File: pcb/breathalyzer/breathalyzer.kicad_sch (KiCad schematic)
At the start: 29 parts, among them J1 Conn_01x07_Pin, J2 MP-3B socket, Q1 Q_PMOS, Q2 NPN, SW1 PTS636SK43SMTR, SW2 430162085826, U1 STM32F030K6Tx, U2 TLV73325PDBV, U4 TLV61070ADBV, U5 AY0438X-L

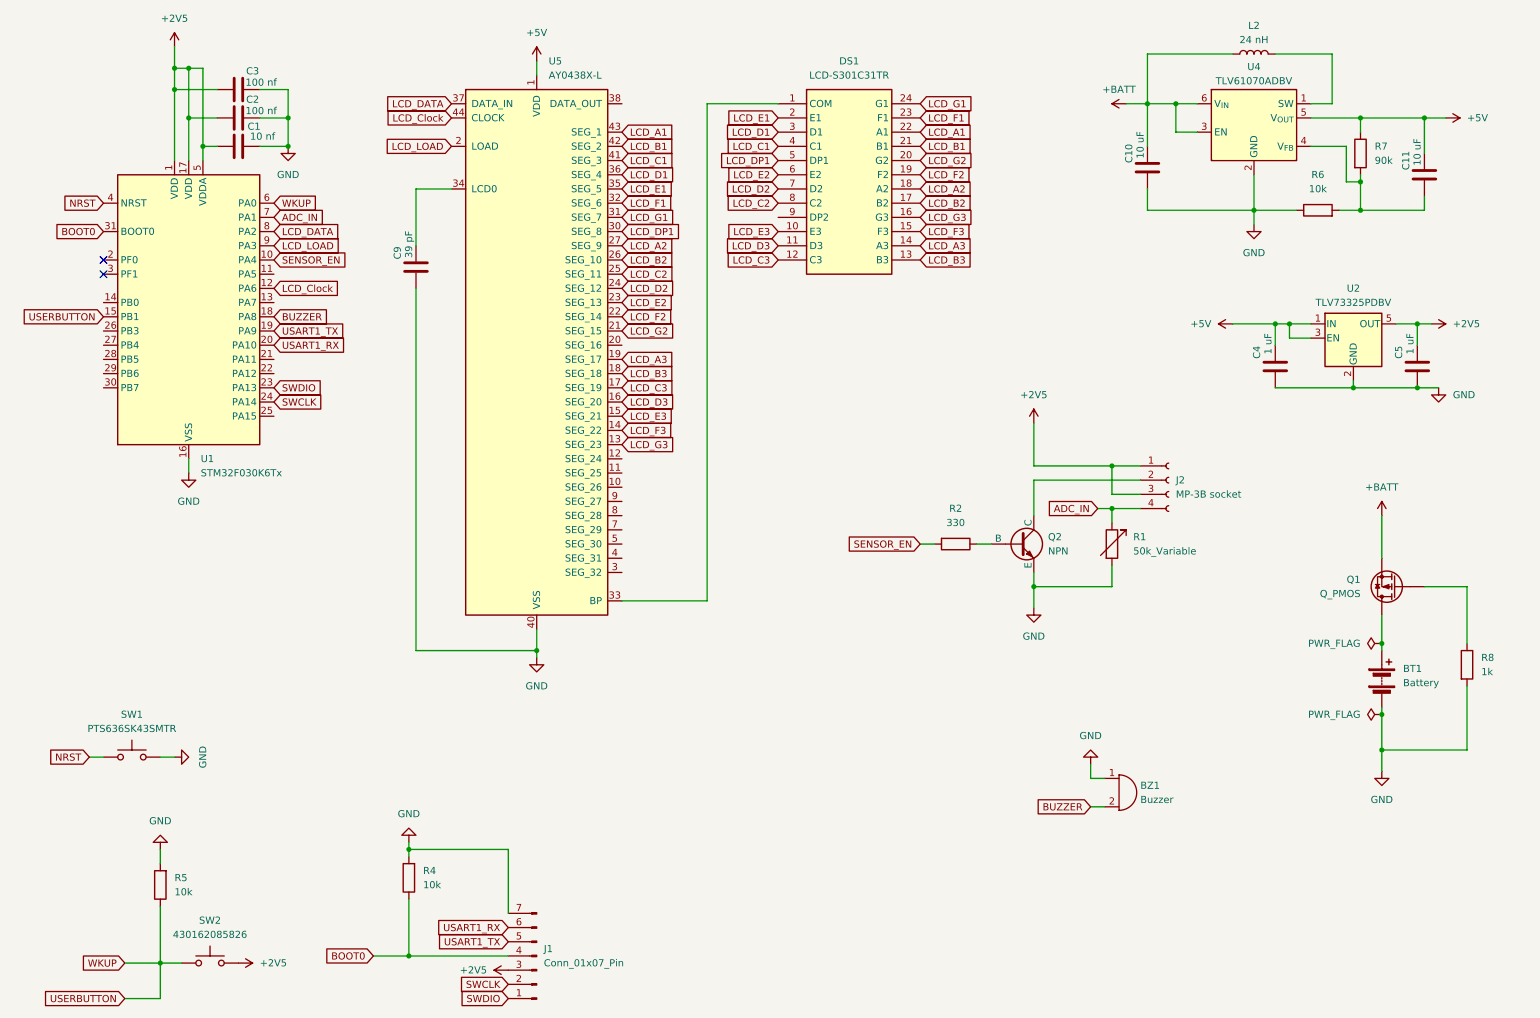
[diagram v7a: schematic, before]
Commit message: finalized schematic
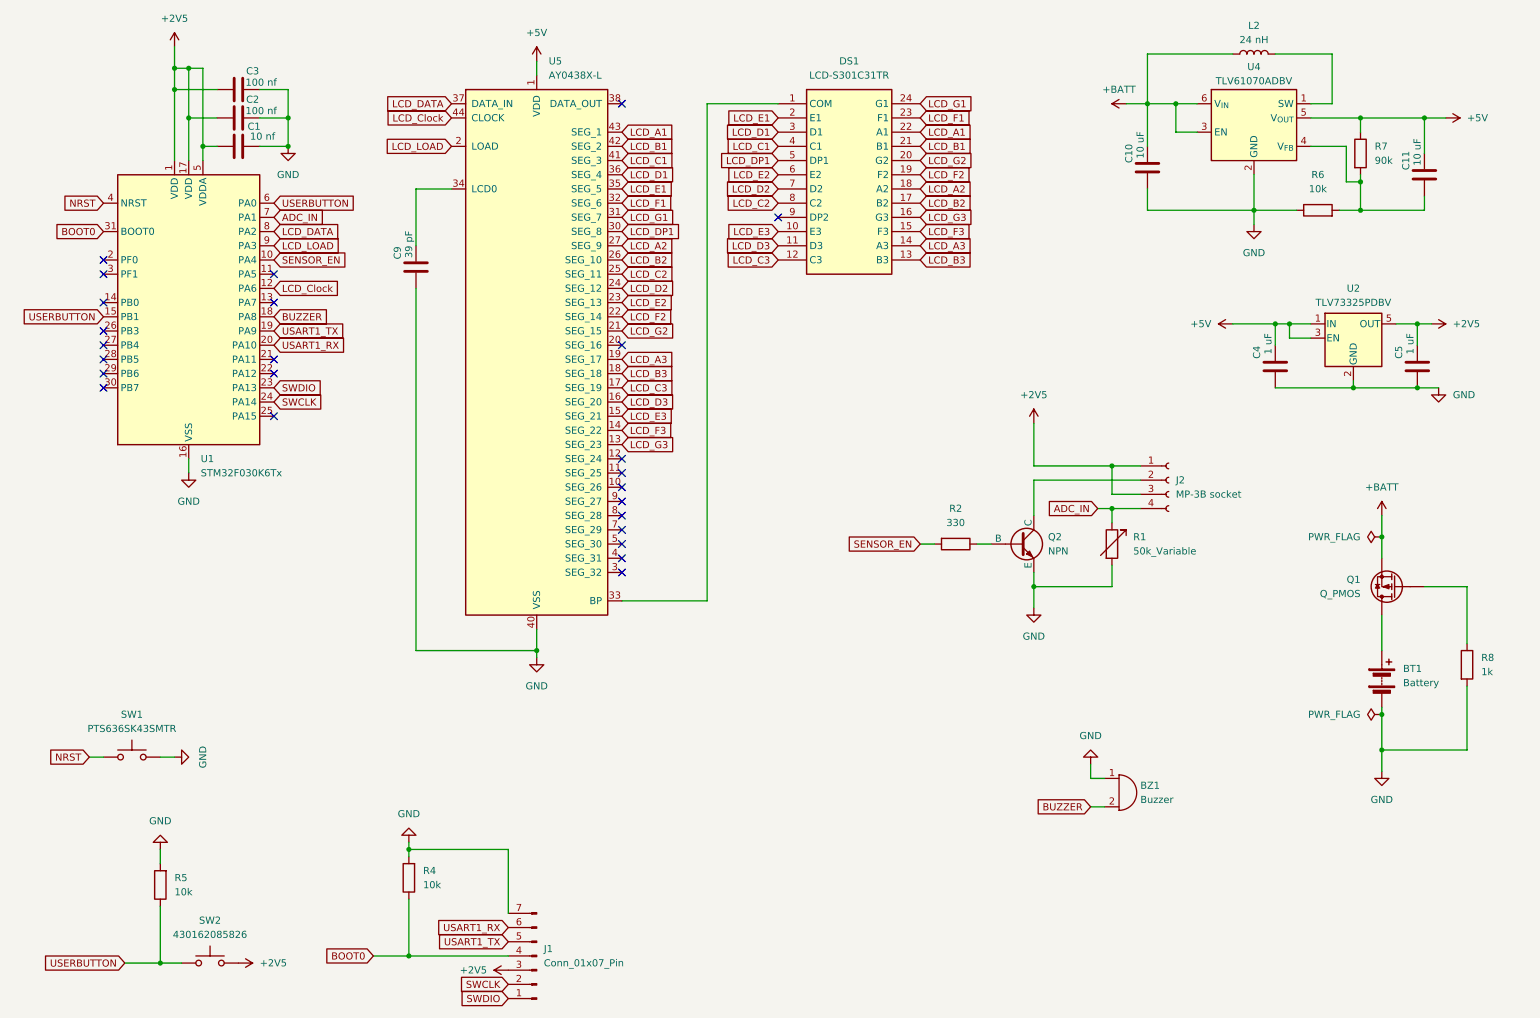
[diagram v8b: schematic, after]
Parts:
- DS1: footprint LCD-S301C31TR -> breathalyzer:LCD-S301C31TR
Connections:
- no-connect marks 2 -> 25
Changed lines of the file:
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@@
 	)
 	(junction
+		(at 257.81 106.68)
+		(diameter 0)
+		(color 0 0 0 0)
+	)
+	(junction
 		(at 195.58 115.57)
 		(diameter 0)
@@
 	)
 	(junction
-		(at 257.81 125.73)
-		(diameter 0)
-		(color 0 0 0 0)
-	)
-	(junction
 		(at 209.55 101.6)
 		(diameter 0)
@@
 	)
 	(no_connect
+		(at 121.92 110.49)
+	)
+	(no_connect
+		(at 121.92 72.39)
+	)
+	(no_connect
+		(at 59.69 77.47)
+	)
+	(no_connect
+		(at 121.92 92.71)
+	)
+	(no_connect
+		(at 121.92 95.25)
+	)
+	(no_connect
 		(at 29.21 59.69)
 	)
 	(no_connect
+		(at 121.92 29.21)
+	)
+	(no_connect
+		(at 29.21 69.85)
+	)
+	(no_connect
+		(at 29.21 72.39)
+	)
+	(no_connect
+		(at 121.92 100.33)
+	)
+	(no_connect
+		(at 149.86 49.53)
+	)
+	(no_connect
+		(at 59.69 59.69)
+	)
+	(no_connect
+		(at 59.69 64.77)
+	)
+	(no_connect
+		(at 121.92 113.03)
+	)
+	(no_connect
+		(at 29.21 64.77)
+	)
+	(no_connect
 		(at 29.21 57.15)
 	)
+	(no_connect
+		(at 59.69 85.09)
+	)
+	(no_connect
+		(at 29.21 77.47)
+	)
+	(no_connect
+		(at 29.21 74.93)
+	)
+	(no_connect
+		(at 59.69 74.93)
+	)
+	(no_connect
+		(at 121.92 107.95)
+	)
+	(no_connect
+		(at 121.92 102.87)
+	)
+	(no_connect
+		(at 121.92 105.41)
+	)
+	(no_connect
+		(at 121.92 97.79)
+	)
+	(no_connect
+		(at 29.21 80.01)
+	)
 	(wire
 		(pts
@@
 	(wire
 		(pts
-			(xy 257.81 125.73) (xy 257.81 127)
-		)
-		(stroke
-			(width 0)
-			(type default)
-		)
-	)
-	(wire
-		(pts
 			(xy 215.9 48.26) (xy 234.95 48.26)
 		)
@@
 	(wire
 		(pts
-			(xy 33.02 182.88) (xy 39.37 182.88)
-		)
-		(stroke
-			(width 0)
-			(type default)
-		)
-	)
-	(wire
-		(pts
 			(xy 39.37 182.88) (xy 43.18 182.88)
 		)
@@
 	(wire
 		(pts
-			(xy 33.02 189.23) (xy 39.37 189.23)
-		)
-		(stroke
-			(width 0)
-			(type default)
-		)
-	)
-	(wire
-		(pts
-			(xy 39.37 189.23) (xy 39.37 182.88)
+			(xy 33.02 182.88) (xy 39.37 182.88)
 		)
 		(stroke
@@
 	(wire
 		(pts
-			(xy 257.81 120.65) (xy 257.81 125.73)
+			(xy 257.81 120.65) (xy 257.81 127)
 		)
 		(stroke
@@
 	(wire
 		(pts
-			(xy 257.81 102.87) (xy 257.81 110.49)
+			(xy 257.81 102.87) (xy 257.81 106.68)
 		)
 		(stroke
@@
 	(wire
 		(pts
+			(xy 257.81 106.68) (xy 257.81 110.49)
+		)
+		(stroke
+			(width 0)
+			(type default)
+		)
+	)
+	(wire
+		(pts
 			(xy 215.9 29.21) (xy 215.9 36.83)
 		)
@@
 		)
 	)
-	(global_label "WKUP"
-		(shape input)
-		(at 33.02 182.88 180)
-		(fields_autoplaced yes)
-		(effects
-			(font
-				(size 1.27 1.27)
-			)
-			(justify right)
-		)
-		(property "Intersheetrefs" "${INTERSHEET_REFS}"
-			(at 24.7129 182.88 0)
-			(effects
-				(font
-					(size 1.27 1.27)
-				)
-				(justify right)
-				(hide yes)
-			)
-		)
-	)
 	(global_label "LCD_B1"
 		(shape input)
@@
 		)
 	)
-	(global_label "WKUP"
-		(shape input)
-		(at 59.69 46.99 0)
-		(fields_autoplaced yes)
-		(effects
-			(font
-				(size 1.27 1.27)
-			)
-			(justify left)
-		)
-		(property "Intersheetrefs" "${INTERSHEET_REFS}"
-			(at 67.9971 46.99 0)
-			(effects
-				(font
-					(size 1.27 1.27)
-				)
-				(justify left)
-				(hide yes)
-			)
-		)
-	)
 	(global_label "LCD_DATA"
 		(shape input)
@@
 		)
 	)
+	(global_label "USERBUTTON"
+		(shape input)
+		(at 59.69 46.99 0)
+		(fields_autoplaced yes)
+		(effects
+			(font
+				(size 1.27 1.27)
+			)
+			(justify left)
+		)
+		(property "Intersheetrefs" "${INTERSHEET_REFS}"
+			(at 74.8309 46.99 0)
+			(effects
+				(font
+					(size 1.27 1.27)
+				)
+				(justify left)
+				(hide yes)
+			)
+		)
+	)
 	(global_label "LCD_DP1"
 		(shape input)
@@
 	(global_label "USERBUTTON"
 		(shape input)
-		(at 33.02 189.23 180)
+		(at 33.02 182.88 180)
 		(fields_autoplaced yes)
 		(effects
@@
 		)
 		(property "Intersheetrefs" "${INTERSHEET_REFS}"
-			(at 17.8791 189.23 0)
+			(at 17.8791 182.88 0)
 			(effects
 				(font
@@
 	)
 	(symbol
+		(lib_id "power:PWR_FLAG")
+		(at 257.81 106.68 90)
+		(unit 1)
+		(exclude_from_sim no)
+		(in_bom yes)
+		(on_board yes)
+		(dnp no)
+		(fields_autoplaced yes)
+		(property "Reference" "#FLG03"
+			(at 255.905 106.68 0)
+			(effects
+				(font
+					(size 1.27 1.27)
+				)
+				(hide yes)
+			)
+		)
+		(property "Value" "PWR_FLAG"
+			(at 254 106.6799 90)
+			(effects
+				(font
+					(size 1.27 1.27)
+				)
+				(justify left)
+			)
+		)
+		(property "Footprint" ""
+			(at 257.81 106.68 0)
+			(effects
+				(font
+					(size 1.27 1.27)
+				)
+				(hide yes)
+			)
+		)
+		(property "Datasheet" "~"
+			(at 257.81 106.68 0)
+			(effects
+				(font
+					(size 1.27 1.27)
+				)
+				(hide yes)
+			)
+		)
+		(property "Description" "Special symbol for telling ERC where power comes from"
+			(at 257.81 106.68 0)
+			(effects
+				(font
+					(size 1.27 1.27)
+				)
+				(hide yes)
+			)
+		)
+		(pin "1"
+		)
+		(instances
+			(project "breathalyzer"
+				(path "/e92d6a20-f7e6-42bc-b7eb-52ddd833ed75"
+					(reference "#FLG03")
+					(unit 1)
+				)
+			)
+		)
+	)
+	(symbol
 		(lib_id "Regulator_Linear:TLV73325PDBV")
 		(at 252.73 71.12 0)
@@
 			)
 		)
-		(property "Footprint" "LCD-S301C31TR"
+		(property "Footprint" "breathalyzer:LCD-S301C31TR"
 			(at 171.45 124.13 0)
 			(effects
@@
 					(unit 1)
 				)
-			)
-		)
-	)
-	(symbol
-		(lib_id "power:PWR_FLAG")
-		(at 257.81 125.73 90)
-		(unit 1)
-		(exclude_from_sim no)
-		(in_bom yes)
-		(on_board yes)
-		(dnp no)
-		(fields_autoplaced yes)
-		(property "Reference" "#FLG01"
-			(at 255.905 125.73 0)
-			(effects
-				(font
-					(size 1.27 1.27)
-				)
-				(hide yes)
-			)
-		)
-		(property "Value" "PWR_FLAG"
-			(at 254 125.7299 90)
-			(effects
-				(font
-					(size 1.27 1.27)
-				)
-				(justify left)
-			)
-		)
-		(property "Footprint" ""
-			(at 257.81 125.73 0)
-			(effects
-				(font
-					(size 1.27 1.27)
-				)
-				(hide yes)
-			)
-		)
-		(property "Datasheet" "~"
-			(at 257.81 125.73 0)
-			(effects
-				(font
-					(size 1.27 1.27)
-				)
-				(hide yes)
-			)
-		)
-		(property "Description" "Special symbol for telling ERC where power comes from"
-			(at 257.81 125.73 0)
-			(effects
-				(font
-					(size 1.27 1.27)
-				)
-				(hide yes)
-			)
-		)
-		(pin "1"
-		)
-		(instances
-			(project ""
-				(path "/e92d6a20-f7e6-42bc-b7eb-52ddd833ed75"
-					(reference "#FLG01")
-					(unit 1)
-				)
